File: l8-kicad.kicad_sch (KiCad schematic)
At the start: 5 parts, among them J3 Screw_Terminal_01x06

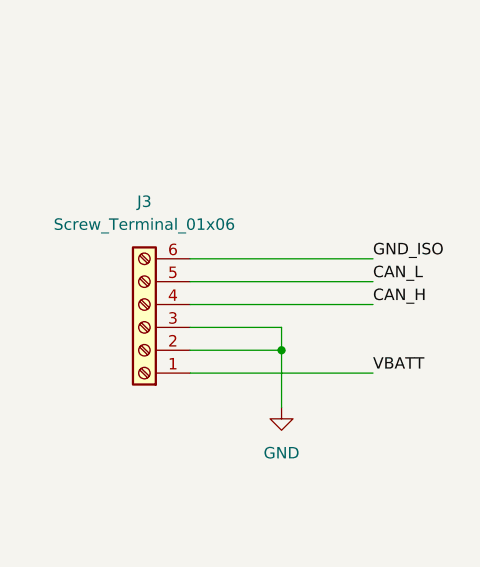
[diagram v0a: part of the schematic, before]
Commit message: remove tp and rotate cpu
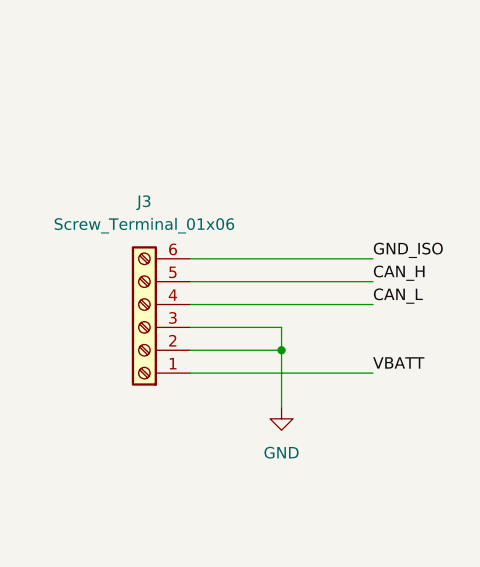
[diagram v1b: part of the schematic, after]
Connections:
- net CAN_H: now also J3.5 (Pin_5); no longer J3.4 (Pin_4)
- net CAN_L: now also J3.4 (Pin_4); no longer J3.5 (Pin_5)
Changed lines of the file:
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@@
 		)
 	)
-	(label "CAN_L"
+	(label "CAN_H"
 		(at 396.24 204.47 0)
 		(fields_autoplaced yes)
@@
 		)
 	)
-	(label "CAN_H"
+	(label "CAN_L"
 		(at 396.24 207.01 0)
 		(fields_autoplaced yes)

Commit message: version 2 changes
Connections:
- net CAN_H: now also J3.4 (Pin_4); no longer J3.5 (Pin_5)
- net CAN_L: now also J3.5 (Pin_5); no longer J3.4 (Pin_4)
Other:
- sheet MCU ports: added SPI4_CS_1, SPI4_CS_2; removed SPI3_CS, SPI3_SCK, SPI3_SDI, SPI3_SDO, SPI4_CS
- note added: "LCD/TOUCH"
- note removed: "LCD"
- note removed: "TOUCH"
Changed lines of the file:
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@@
+	(wire
+		(pts
+			(xy 222.25 203.2) (xy 212.09 203.2)
+		)
+		(stroke
+			(width 0)
+			(type default)
+		)
+	)
 	(wire
 		(pts
@@
 	(wire
 		(pts
+			(xy 222.25 205.74) (xy 212.09 205.74)
+		)
+		(stroke
+			(width 0)
+			(type default)
+		)
+	)
+	(wire
+		(pts
+			(xy 212.09 232.41) (xy 222.25 232.41)
+		)
+		(stroke
+			(width 0)
+			(type default)
+		)
+	)
+	(wire
+		(pts
+			(xy 222.25 210.82) (xy 212.09 210.82)
+		)
+		(stroke
+			(width 0)
+			(type default)
+		)
+	)
+	(wire
+		(pts
 			(xy 375.92 212.09) (xy 386.08 212.09)
 		)
@@
 	(wire
 		(pts
+			(xy 212.09 224.79) (xy 222.25 224.79)
+		)
+		(stroke
+			(width 0)
+			(type default)
+		)
+	)
+	(wire
+		(pts
+			(xy 212.09 227.33) (xy 222.25 227.33)
+		)
+		(stroke
+			(width 0)
+			(type default)
+		)
+	)
+	(wire
+		(pts
+			(xy 212.09 200.66) (xy 222.25 200.66)
+		)
+		(stroke
+			(width 0)
+			(type default)
+		)
+	)
+	(wire
+		(pts
 			(xy 375.92 201.93) (xy 396.24 201.93)
+		)
+		(stroke
+			(width 0)
+			(type default)
+		)
+	)
+	(wire
+		(pts
+			(xy 212.09 215.9) (xy 222.25 215.9)
 		)
 		(stroke
@@
 		)
 	)
+	(wire
+		(pts
+			(xy 212.09 229.87) (xy 222.25 229.87)
+		)
+		(stroke
+			(width 0)
+			(type default)
+		)
+	)
+	(wire
+		(pts
+			(xy 222.25 213.36) (xy 212.09 213.36)
+		)
+		(stroke
+			(width 0)
+			(type default)
+		)
+	)
 	(text "ST_SENSOR"
 		(exclude_from_sim no)
@@
 		)
 	)
-	(text "LCD"
-		(exclude_from_sim no)
-		(at 236.22 172.72 0)
-		(effects
-			(font
-				(size 1.27 1.27)
-			)
-		)
-	)
 	(text "IIS3DHHCTR"
 		(exclude_from_sim no)
@@
 		)
 	)
-	(text "TOUCH"
+	(text "LCD/TOUCH"
 		(exclude_from_sim no)
-		(at 236.22 208.28 0)
-		(effects
-			(font
-				(size 1.27 1.27)
-			)
+		(at 243.332 214.63 0)
+		(effects
+			(font
+				(size 1.27 1.27)
+			)
+		)
+	)
+	(label "SPI4_CS_1"
+		(at 222.25 213.36 0)
+		(effects
+			(font
+				(size 1.27 1.27)
+			)
+			(justify left bottom)
 		)
 	)
@@
 	)
 	(label "LCD_RESET"
-		(at 212.09 187.96 0)
+		(at 222.25 232.41 0)
 		(fields_autoplaced yes)
 		(effects
@@
 		)
 	)
-	(label "CAN_H"
+	(label "CAN_L"
 		(at 396.24 204.47 0)
 		(fields_autoplaced yes)
@@
 	)
 	(label "LCD_ON"
-		(at 212.09 180.34 0)
+		(at 222.25 224.79 0)
 		(fields_autoplaced yes)
 		(effects
@@
 		)
 	)
-	(label "SPI4_CS"
-		(at 212.09 208.28 0)
-		(fields_autoplaced yes)
-		(effects
-			(font
-				(size 1.27 1.27)
-			)
-			(justify left bottom)
-		)
-	)
 	(label "SPI4_SDI"
-		(at 212.09 205.74 0)
-		(fields_autoplaced yes)
-		(effects
-			(font
-				(size 1.27 1.27)
-			)
-			(justify left bottom)
-		)
-	)
-	(label "SPI3_SDI"
+		(at 222.25 205.74 0)
+		(fields_autoplaced yes)
+		(effects
+			(font
+				(size 1.27 1.27)
+			)
+			(justify left bottom)
+		)
+	)
+	(label "SPI4_SDI"
 		(at 95.25 68.58 0)
 		(fields_autoplaced yes)
@@
 	)
 	(label "LCD_DC"
-		(at 212.09 182.88 0)
+		(at 222.25 227.33 0)
 		(fields_autoplaced yes)
 		(effects
@@
 		)
 	)
-	(label "SPI3_CS"
+	(label "SPI4_CS_2"
 		(at 95.25 73.66 0)
 		(fields_autoplaced yes)
@@
 	)
 	(label "LCD_LED"
-		(at 212.09 185.42 0)
+		(at 222.25 229.87 0)
 		(fields_autoplaced yes)
 		(effects
@@
 		)
 	)
-	(label "SPI3_SDI"
-		(at 212.09 175.26 0)
-		(fields_autoplaced yes)
-		(effects
-			(font
-				(size 1.27 1.27)
-			)
-			(justify left bottom)
-		)
-	)
 	(label "CAN_L"
 		(at 53.34 135.89 180)
@@
 		)
 	)
-	(label "SPI4_CS"
+	(label "SPI4_CS_1"
 		(at 95.25 95.25 0)
 		(fields_autoplaced yes)
@@
 		)
 	)
-	(label "SPI3_SDO"
+	(label "SPI4_SDO"
 		(at 95.25 71.12 0)
 		(fields_autoplaced yes)
@@
 		)
 	)
-	(label "SPI3_SCK"
-		(at 212.09 170.18 0)
-		(fields_autoplaced yes)
-		(effects
-			(font
-				(size 1.27 1.27)
-			)
-			(justify left bottom)
-		)
-	)
-	(label "SPI3_SDO"
-		(at 212.09 172.72 0)
-		(fields_autoplaced yes)
-		(effects
-			(font
-				(size 1.27 1.27)
-			)
-			(justify left bottom)
-		)
-	)
 	(label "SPI4_SCK"
-		(at 212.09 200.66 0)
+		(at 222.25 200.66 0)
 		(fields_autoplaced yes)
 		(effects
@@
 	)
 	(label "SPI4_IRQ"
-		(at 212.09 210.82 0)
+		(at 222.25 210.82 0)
 		(fields_autoplaced yes)
 		(effects
@@
 		)
 	)
-	(label "SPI3_SCK"
+	(label "SPI4_SCK"
 		(at 95.25 66.04 0)
 		(fields_autoplaced yes)
@@
 	)
 	(label "SPI4_SDO"
-		(at 212.09 203.2 0)
+		(at 222.25 203.2 0)
 		(fields_autoplaced yes)
 		(effects
@@
 		)
 	)
-	(label "CAN_L"
+	(label "CAN_H"
 		(at 396.24 207.01 0)
 		(fields_autoplaced yes)
@@
 		)
 	)
+	(label "SPI4_CS_2"
+		(at 222.25 215.9 0)
+		(effects
+			(font
+				(size 1.27 1.27)
+			)
+			(justify left bottom)
+		)
+	)
 	(label "SPI2_IRQ2"
 		(at 92.71 250.19 0)
@@
 	(label "SPI2_IRQ"
 		(at 212.09 158.75 0)
-		(fields_autoplaced yes)
-		(effects
-			(font
-				(size 1.27 1.27)
-			)
-			(justify left bottom)
-		)
-	)
-	(label "SPI3_CS"
-		(at 212.09 177.8 0)
 		(fields_autoplaced yes)
 		(effects
@@
 	)
 	(symbol
-		(lib_id "l8-kicad-rescue:GND-power")
+		(lib_id "power:GND")
 		(at 386.08 218.44 0)
 		(unit 1)
@@
 			)
 		)
-		(pin "SPI3_SDO" input
-			(at 212.09 172.72 0)
-			(effects
-				(font
-					(size 1.27 1.27)
-				)
-				(justify right)
-			)
-		)
-		(pin "SPI3_SCK" output
-			(at 212.09 170.18 0)
-			(effects
-				(font
-					(size 1.27 1.27)
-				)
-				(justify right)
-			)
-		)
-		(pin "SPI3_SDI" output
-			(at 212.09 175.26 0)
-			(effects
-				(font
-					(size 1.27 1.27)
-				)
-				(justify right)
-			)
-		)
 		(pin "SPI4_SDI" input
 			(at 212.09 205.74 0)
@@
 			)
 		)
-		(pin "SPI4_CS" output
-			(at 212.09 208.28 0)
-			(effects
-				(font
-					(size 1.27 1.27)
-				)
-				(justify right)
-			)
-		)
 		(pin "SPI4_IRQ" input
 			(at 212.09 210.82 0)
@@
 		)
 		(pin "LCD_ON" output
-			(at 212.09 180.34 0)
+			(at 212.09 224.79 0)
 			(effects
 				(font
@@
 			)
 		)
-		(pin "SPI3_CS" output
-			(at 212.09 177.8 0)
-			(effects
-				(font
-					(size 1.27 1.27)
-				)
-				(justify right)
-			)
-		)
 		(pin "CAN1_TX" output
 			(at 180.34 227.33 180)
@@
 		)
 		(pin "LCD_DC" output
-			(at 212.09 182.88 0)
+			(at 212.09 227.33 0)
 			(effects
 				(font
@@
 		)
 		(pin "LCD_LED" output
-			(at 212.09 185.42 0)
+			(at 212.09 229.87 0)
 			(effects
 				(font
@@
 		)
 		(pin "LCD_RESET" output
-			(at 212.09 187.96 0)
+			(at 212.09 232.41 0)
 			(effects
 				(font
@@
 			)
 		)
+		(pin "SPI4_CS_1" output
+			(at 212.09 213.36 0)
+			(effects
+				(font
+					(size 1.27 1.27)
+				)
+				(justify right)
+			)
+		)
+		(pin "SPI4_CS_2" output
+			(at 212.09 215.9 0)
+			(effects
+				(font
+					(size 1.27 1.27)
+				)
+				(justify right)
+			)
+		)

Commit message: 5v buck
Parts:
- added J6: JST GH, dnt:JST_GH_BM06B-GHS-TBT_1x06-1MP_P1.25mm_Vertical, symbol PCM_SL_Connectors:JST_06
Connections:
- net CAN_H: now also J6.4
- net CAN_L: now also J6.5
- net GND: now also J6.2, J6.3
- net GND_ISO: now also J6.6
- net VBATT: now also J6.1

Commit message: version 2 initial
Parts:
- removed J3: Screw_Terminal_01x06, TerminalBlock_Phoenix:TerminalBlock_Phoenix_PT-1,5-6-3.5-H_1x06_P3.50mm_Horizontal, symbol Connector:Screw_Terminal_01x06
- removed J6: JST GH, dnt:JST_GH_BM06B-GHS-TBT_1x06-1MP_P1.25mm_Vertical, symbol PCM_SL_Connectors:JST_06
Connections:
- no-connect marks 0 -> 1
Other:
- sheet MCU ports: added SPI3_CS, SPI3_SCK, SPI3_SDI, SPI3_SDO, SYS_WAKEUP; removed none
- sheet can ports: added VBATT; removed CAN_H, CAN_L
- sheet lcd ports: added SD_CS, SD_SCK, SD_SDI, SD_SDO, _T_IRQ; removed T_CLK, T_IRQ, T_SDI, T_SDO

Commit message: update to version 9 on selwyn
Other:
- company: (none) -> DNT
- title: (none) -> l8
